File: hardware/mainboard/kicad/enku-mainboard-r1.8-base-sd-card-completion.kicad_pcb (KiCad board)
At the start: 4 copper layers, 59 x 101 mm, 125 parts, among them J1 1S LiPo + NTC, J2 Hirose DM3AT-SF-PEJM5, J3 FH34SRJ-24S-0.5SH(50), J5 GCT USB4105-GF-A-120, J6 4-pin pogo dock, J7 Tag-Connect TC2030-IDC-NL, Q1 IRLML6346TRPBF, Q2 AO3401A, SW1 HARD POWER, SW2 BOOT / RECOVERY, SW3 BTN_L1, SW4 BTN_L2, SW5 BTN_R1, SW6 BTN_R2, U1 ESP32-S3-WROOM-1-N16R8, U2 TPS2121, U3 BQ25185DLHR, U4 TPS63802DLAR, U5 BMI270, U8 USBLC6-2SC6, U9 TMUX1101DBVR

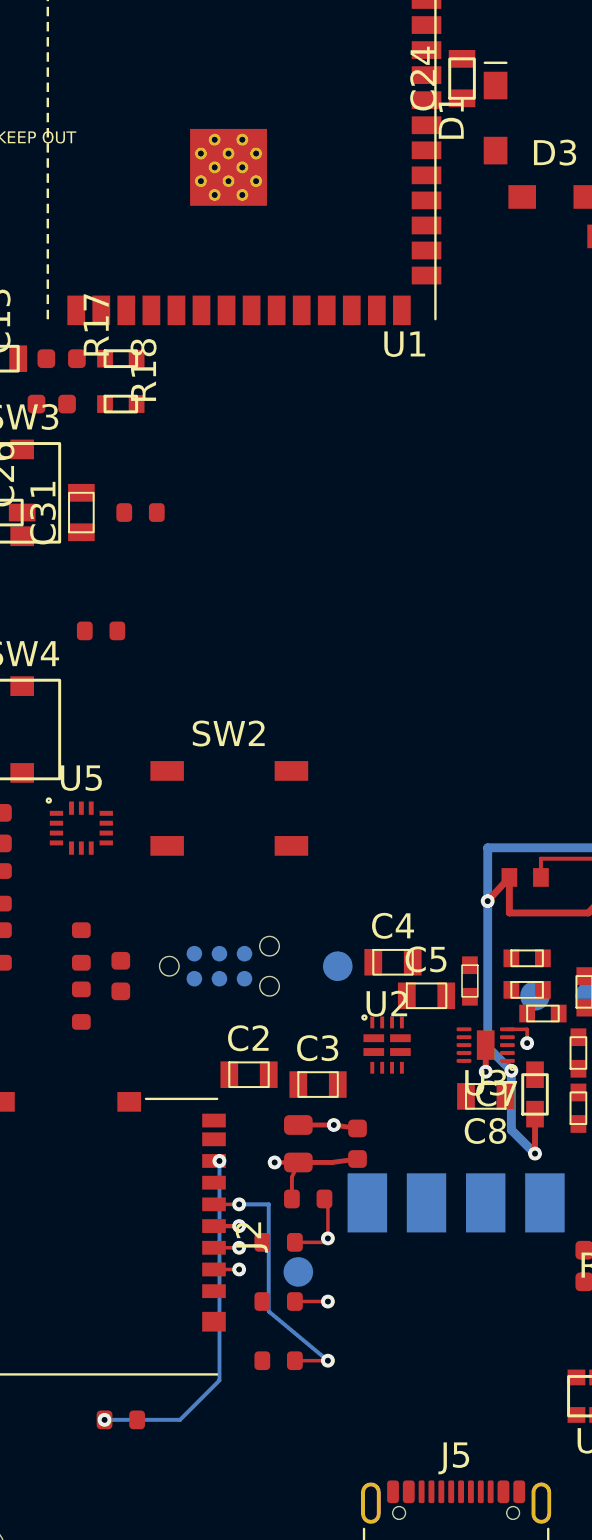
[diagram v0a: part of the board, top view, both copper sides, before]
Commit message: R41: connect all four MCU SPI nets to microSD resistor network with outboard MCU vias
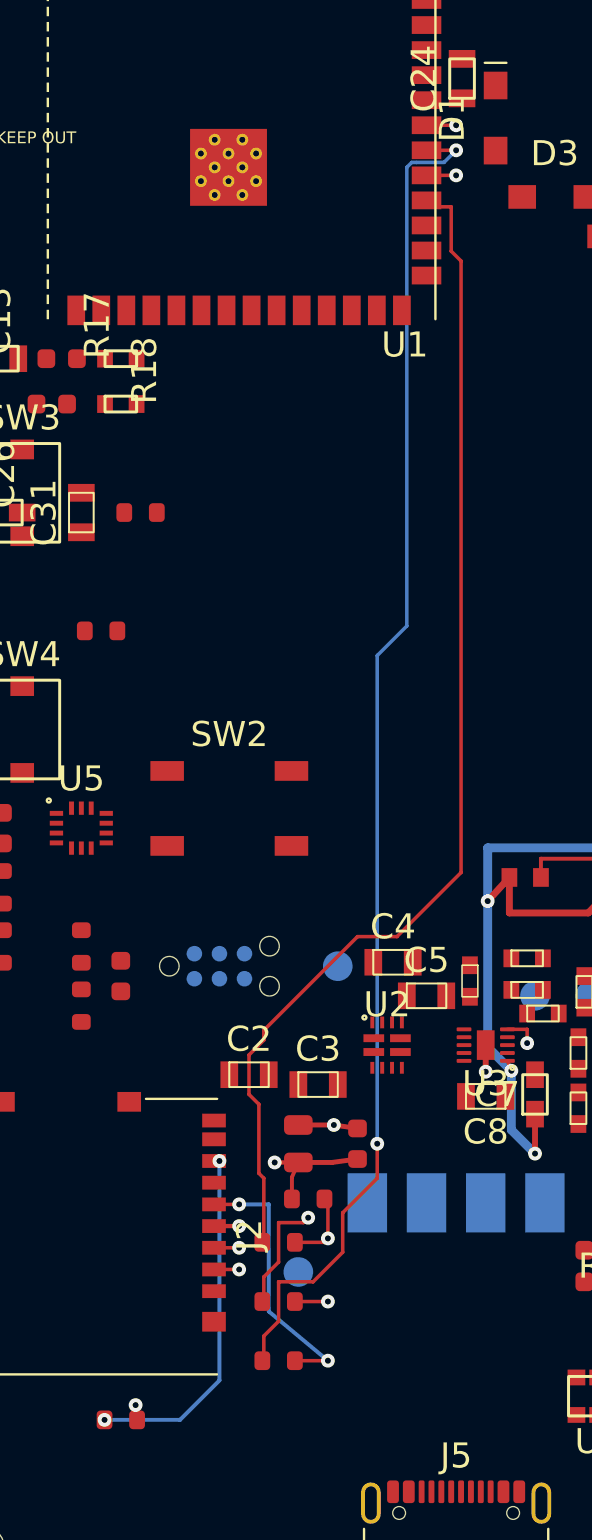
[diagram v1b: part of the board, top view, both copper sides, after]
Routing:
- net SPI_MISO: track 0.00 -> 73.9 mm, vias 0 -> 2
- net SPI_SCLK: track 0.00 -> 68.9 mm, vias 0 -> 2
- net SPI_MOSI: track 0.00 -> 63.4 mm, vias 0 -> 2
- net SD_CS: track 0.00 -> 60.0 mm
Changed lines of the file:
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@@
   (via (at 35 96.875) (size 0.70) (drill 0.30) (layers "F.Cu" "B.Cu") (net 12))
   (via (at 29.175 110) (size 0.70) (drill 0.30) (layers "F.Cu" "B.Cu") (net 12))
+  (segment (start 45.5 48.25) (end 45.75 48.5) (width 0.18) (layer "F.Cu") (net 60))
+  (segment (start 45.75 48.5) (end 46.75 48.5) (width 0.18) (layer "F.Cu") (net 60))
+  (segment (start 46.75 48.5) (end 46.75 50.75) (width 0.18) (layer "F.Cu") (net 60))
+  (segment (start 46.75 50.75) (end 47.25 51.25) (width 0.18) (layer "F.Cu") (net 60))
+  (segment (start 47.25 51.25) (end 47.25 82.25) (width 0.18) (layer "F.Cu") (net 60))
+  (segment (start 47.25 82.25) (end 44.0 85.5) (width 0.18) (layer "F.Cu") (net 60))
+  (segment (start 44.0 85.5) (end 42.0 85.5) (width 0.18) (layer "F.Cu") (net 60))
+  (segment (start 42.0 85.5) (end 37.25 90.25) (width 0.18) (layer "F.Cu") (net 60))
+  (segment (start 37.25 90.25) (end 37.25 90.75) (width 0.18) (layer "F.Cu") (net 60))
+  (segment (start 37.25 90.75) (end 36.5 91.5) (width 0.18) (layer "F.Cu") (net 60))
+  (segment (start 36.5 91.5) (end 36.5 93.5) (width 0.18) (layer "F.Cu") (net 60))
+  (segment (start 36.5 93.5) (end 37.0 94.0) (width 0.18) (layer "F.Cu") (net 60))
+  (segment (start 37.0 94.0) (end 37.0 97.5) (width 0.18) (layer "F.Cu") (net 60))
+  (segment (start 37.0 97.5) (end 37.25 97.75) (width 0.18) (layer "F.Cu") (net 60))
+  (segment (start 37.25 97.75) (end 37.25 101.0) (width 0.18) (layer "F.Cu") (net 60))
+  (segment (start 47 46.905) (end 45.5 48.405) (width 0.18) (layer "In1.Cu") (net 61))
+  (segment (start 45.5 48.405) (end 45.5 71.25) (width 0.18) (layer "In1.Cu") (net 61))
+  (segment (start 45.5 71.25) (end 39.5 77.25) (width 0.18) (layer "In1.Cu") (net 61))
+  (segment (start 39.5 77.25) (end 39.5 99.75) (width 0.18) (layer "In1.Cu") (net 61))
+  (segment (start 39.5 99.75) (end 39.25 100.0) (width 0.18) (layer "F.Cu") (net 61))
+  (segment (start 39.25 100.0) (end 38.0 100.0) (width 0.18) (layer "F.Cu") (net 61))
+  (segment (start 38.0 100.0) (end 38.0 102.0) (width 0.18) (layer "F.Cu") (net 61))
+  (segment (start 38.0 102.0) (end 37.25 102.75) (width 0.18) (layer "F.Cu") (net 61))
+  (segment (start 37.25 102.75) (end 37.25 104.0) (width 0.18) (layer "F.Cu") (net 61))
+  (via (at 47 46.905) (size 0.70) (drill 0.30) (layers "F.Cu" "B.Cu") (net 61))
+  (via (at 39.5 99.75) (size 0.70) (drill 0.30) (layers "F.Cu" "B.Cu") (net 61))
+  (segment (start 47 45.635) (end 46.385 46.25) (width 0.18) (layer "B.Cu") (net 62))
+  (segment (start 46.385 46.25) (end 45.0 46.25) (width 0.18) (layer "B.Cu") (net 62))
+  (segment (start 45.0 46.25) (end 44.75 46.25) (width 0.18) (layer "B.Cu") (net 62))
+  (segment (start 44.75 46.25) (end 44.5 46.5) (width 0.18) (layer "B.Cu") (net 62))
+  (segment (start 44.5 46.5) (end 44.5 69.75) (width 0.18) (layer "B.Cu") (net 62))
+  (segment (start 44.5 69.75) (end 43.0 71.25) (width 0.18) (layer "B.Cu") (net 62))
+  (segment (start 43.0 71.25) (end 43.0 96.0) (width 0.18) (layer "B.Cu") (net 62))
+  (segment (start 43.0 96.0) (end 43.0 97.75) (width 0.18) (layer "F.Cu") (net 62))
+  (segment (start 43.0 97.75) (end 41.25 99.5) (width 0.18) (layer "F.Cu") (net 62))
+  (segment (start 41.25 99.5) (end 41.25 101.5) (width 0.18) (layer "F.Cu") (net 62))
+  (segment (start 41.25 101.5) (end 39.75 103.0) (width 0.18) (layer "F.Cu") (net 62))
+  (segment (start 39.75 103.0) (end 38.0 103.0) (width 0.18) (layer "F.Cu") (net 62))
+  (segment (start 38.0 103.0) (end 38.0 105.0) (width 0.18) (layer "F.Cu") (net 62))
+  (segment (start 38.0 105.0) (end 37.25 105.75) (width 0.18) (layer "F.Cu") (net 62))
+  (segment (start 37.25 105.75) (end 37.25 107.0) (width 0.18) (layer "F.Cu") (net 62))
+  (via (at 47 45.635) (size 0.70) (drill 0.30) (layers "F.Cu" "B.Cu") (net 62))
+  (via (at 43.0 96.0) (size 0.70) (drill 0.30) (layers "F.Cu" "B.Cu") (net 62))
+  (segment (start 45.5 44.365) (end 47 44.365) (width 0.18) (layer "F.Cu") (net 63))
+  (segment (start 47 44.365) (end 44.75 46.615) (width 0.18) (layer "In1.Cu") (net 63))
+  (segment (start 44.75 46.615) (end 44.75 68.5) (width 0.18) (layer "In1.Cu") (net 63))
+  (segment (start 44.75 68.5) (end 30.75 82.5) (width 0.18) (layer "In1.Cu") (net 63))
+  (segment (start 30.75 82.5) (end 30.75 109.25) (width 0.18) (layer "In1.Cu") (net 63))
+  (segment (start 30.75 109.25) (end 30.75 110.0) (width 0.18) (layer "F.Cu") (net 63))
+  (via (at 47 44.365) (size 0.70) (drill 0.30) (layers "F.Cu" "B.Cu") (net 63))
+  (via (at 30.75 109.25) (size 0.70) (drill 0.30) (layers "F.Cu" "B.Cu") (net 63))
+  (segment (start 45.5 46.905) (end 47 46.905) (width 0.18) (layer "F.Cu") (net 61))
+  (segment (start 45.5 45.635) (end 47 45.635) (width 0.18) (layer "F.Cu") (net 62))
 )

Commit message: R41: implement switched-rail fail-safe VBUS comparator, discharge model, SD supply and dual ground references
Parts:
- added C38: 100nF 10V, Capacitor_SMD:C_0603_1608Metric, F.Cu at (60.0, 65.0)
- added C39: 1nF C0G 10V, Capacitor_SMD:C_0603_1608Metric, F.Cu at (66.0, 76.0)
- added R70: 26.7k 0.1% 25ppm, Resistor_SMD:R_0603_1608Metric, F.Cu at (66.0, 64.0)
- added R71: 10k 0.1% 25ppm, Resistor_SMD:R_0603_1608Metric, F.Cu at (66.0, 67.0)
- added R72: 100k, Resistor_SMD:R_0603_1608Metric, F.Cu at (66.0, 70.0)
- added R73: 3.3k 1%, Resistor_SMD:R_0603_1608Metric, F.Cu at (66.0, 73.0)
- added U10: TLV3012BIDBVR, ENKU:TLV3012B_DBV0006A, F.Cu at (60.0, 69.0)
- C2: value 10uF 10V -> 1uF 10V
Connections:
- U1 pad 10: (no net) -> USB_VBUS_VALID
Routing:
- net 3V3_SYS: track 36.2 -> 101.8 mm, vias 5 -> 11
- net USB_VBUS_VALID: track 0.00 -> 54.8 mm, vias 0 -> 2
- net VBUS_USB: track 0.00 -> 53.0 mm, vias 0 -> 4
- net GND: track 13.6 -> 43.0 mm, vias 8 -> 15
- net USB_VBUS_DIV: track 0.00 -> 25.0 mm
- net USB_VBUS_REF: track 0.00 -> 1.00 mm
- added copper zone on In1.Cu, net GND
